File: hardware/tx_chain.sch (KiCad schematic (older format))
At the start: 28 parts

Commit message: honed multiple schematics
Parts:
- added D? (x2): BAT83, symbol D_Schottky
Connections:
- net +Vlogic: now also D?.1 (K)
- net GND: now also D?.2 (A); no longer T?.4 (SB)
- net joku_adc: now also C?.1
- net at C?.1, C?.1, T?.5 (SC): now also T?.4 (SB)
- net at Q?.3 (S), R?.1, R?.1: no longer C?.1
- new net: D?.1 (K), D?.2 (A)
- no-connect marks 0 -> 1
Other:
- moved on the sheet: C?, D?, L?, Q?, R?, T?, U?

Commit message: Added RX chain. also modified and cleand up other schemas
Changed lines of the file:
@@
 $Descr A4 11693 8268
 encoding utf-8
-Sheet 5 5
-Title ""
-Date ""
-Rev ""
-Comp ""
-Comment1 ""
+Sheet 5 7
+Title "TX chain"
+Date "2016-09-22"
+Rev "0.1"
+Comp "PRK - OH2TI"
+Comment1 "exla - OH2EHK"
 Comment2 ""
 Comment3 ""
@@
 	3250 3950 3250 4650
 Wire Wire Line
-	3050 4650 3250 4650
-Wire Wire Line
-	3250 4650 3950 4650
+	3050 4650 3950 4650
 Wire Wire Line
 	3050 4450 3400 4450
@@
 	3400 4450 3400 3750
 Wire Wire Line
-	3050 3750 3400 3750
-Wire Wire Line
-	3400 3750 3950 3750
-$Comp
-L GND #PWR?
+	3050 3750 3950 3750
+$Comp
+L GND #PWR018
 U 1 1 57E4343C
 P 3100 4100
-F 0 "#PWR?" H 3100 3850 50  0001 C CNN
+F 0 "#PWR018" H 3100 3850 50  0001 C CNN
 F 1 "GND" H 3100 3950 50  0000 C CNN
 F 2 "" H 3100 4100 50  0000 C CNN
@@
 	3100 3850 3100 4100
 $Comp
-L GND #PWR?
+L GND #PWR019
 U 1 1 57E4345E
 P 3100 4800
-F 0 "#PWR?" H 3100 4550 50  0001 C CNN
+F 0 "#PWR019" H 3100 4550 50  0001 C CNN
 F 1 "GND" H 3100 4650 50  0000 C CNN
 F 2 "" H 3100 4800 50  0000 C CNN
@@
 	1750 3750 2250 3750
 $Comp
-L +Vlogic #PWR?
+L +Vlogic #PWR020
 U 1 1 57E434AC
 P 2150 3550
-F 0 "#PWR?" H 2150 3350 50  0001 C CNN
+F 0 "#PWR020" H 2150 3350 50  0001 C CNN
 F 1 "+Vlogic" H 2150 3750 50  0000 C CNN
 F 2 "" H 2150 3550 50  0000 C CNN
@@
 $EndComp
 $Comp
-L +Vlogic #PWR?
+L +Vlogic #PWR021
 U 1 1 57E434C4
 P 2150 4250
-F 0 "#PWR?" H 2150 4050 50  0001 C CNN
+F 0 "#PWR021" H 2150 4050 50  0001 C CNN
 F 1 "+Vlogic" H 2150 4450 50  0000 C CNN
 F 2 "" H 2150 4250 50  0000 C CNN
@@
 $EndComp
 Wire Wire Line
-	3550 4100 3750 4100
-Wire Wire Line
-	3750 4100 3950 4100
-Wire Wire Line
-	3950 4100 3950 4150
-Wire Wire Line
-	3950 4150 3950 4350
+	3550 4100 3950 4100
+Wire Wire Line
+	3950 4100 3950 4350
 Connection ~ 3750 4100
 Connection ~ 3750 4400
 $Comp
-L GND #PWR?
+L GND #PWR022
 U 1 1 57E43B57
 P 3650 4450
-F 0 "#PWR?" H 3650 4200 50  0001 C CNN
+F 0 "#PWR022" H 3650 4200 50  0001 C CNN
 F 1 "GND" H 3650 4300 50  0000 C CNN
 F 2 "" H 3650 4450 50  0000 C CNN
@@
 Connection ~ 3650 4400
 $Comp
-L GND #PWR?
+L GND #PWR023
 U 1 1 57E43B98
 P 5100 4800
-F 0 "#PWR?" H 5100 4550 50  0001 C CNN
+F 0 "#PWR023" H 5100 4550 50  0001 C CNN
 F 1 "GND" H 5100 4650 50  0000 C CNN
 F 2 "" H 5100 4800 50  0000 C CNN
@@
 $EndComp
 Wire Wire Line
-	4750 4450 5100 4450
-Wire Wire Line
-	5100 4450 5700 4450
+	4750 4450 5700 4450
 Wire Wire Line
 	5700 4150 5700 4050
 Wire Wire Line
-	5600 4050 5700 4050
-Wire Wire Line
-	5700 4050 5800 4050
+	5600 4050 5800 4050
 $Comp
 L C C?
@@
 $EndComp
 Wire Wire Line
-	6100 4050 6200 4050
-Wire Wire Line
-	6200 4050 6300 4050
+	6100 4050 6300 4050
 $Comp
 L R R?
@@
 Connection ~ 5100 4450
 $Comp
-L GND #PWR?
+L GND #PWR024
 U 1 1 57E44284
 P 6600 4800
-F 0 "#PWR?" H 6600 4550 50  0001 C CNN
+F 0 "#PWR024" H 6600 4550 50  0001 C CNN
 F 1 "GND" H 6600 4650 50  0000 C CNN
 F 2 "" H 6600 4800 50  0000 C CNN
@@
 	6600 4350 6600 4250
 $Comp
-L Vin #Vin?
+L Vin #Vin025
 U 1 1 57E4514D
 P 6600 3050
-F 0 "#Vin?" H 6750 3100 60  0001 C CNN
+F 0 "#Vin025" H 6750 3100 60  0001 C CNN
 F 1 "Vin" H 6450 3100 60  0000 C CNN
 F 2 "" H 6600 3050 60  0001 C CNN
@@
 $EndComp
 $Comp
-L GND #PWR?
+L GND #PWR026
 U 1 1 57E451F7
 P 6850 3550
-F 0 "#PWR?" H 6850 3300 50  0001 C CNN
+F 0 "#PWR026" H 6850 3300 50  0001 C CNN
 F 1 "GND" H 6850 3400 50  0000 C CNN
 F 2 "" H 6850 3550 50  0000 C CNN
@@
 	6850 3500 6850 3550
 Wire Wire Line
-	6600 3500 6600 3800
-Wire Wire Line
-	6600 3800 6600 3850
+	6600 3500 6600 3850
 $Comp
 L C C?
@@
 $EndComp
 Wire Wire Line
-	7850 3800 7950 3800
-Wire Wire Line
-	7950 3800 8050 3800
+	7850 3800 8050 3800
 Wire Wire Line
 	7950 3800 7950 4050
 Wire Wire Line
-	7350 3800 7450 3800
-Wire Wire Line
-	7450 3800 7550 3800
+	7350 3800 7550 3800
 $Comp
 L R R?
@@
 Connection ~ 7950 3800
 Wire Wire Line
-	8100 3500 8350 3500
-Wire Wire Line
-	8350 3500 9100 3500
-Wire Wire Line
-	9100 3500 9200 3500
-Wire Wire Line
-	8350 3400 8350 3500
-Wire Wire Line
-	8350 3500 8350 3600
+	8100 3500 9200 3500
+Wire Wire Line
+	8350 3400 8350 3600
 $Comp
 L INDUCTOR L?
@@
 $EndComp
 $Comp
-L GND #PWR?
+L GND #PWR027
 U 1 1 57E458EE
 P 8100 3150
-F 0 "#PWR?" H 8100 2900 50  0001 C CNN
+F 0 "#PWR027" H 8100 2900 50  0001 C CNN
 F 1 "GND" H 8100 3000 50  0000 C CNN
 F 2 "" H 8100 3150 50  0000 C CNN
@@
 $EndComp
 $Comp
-L Vin #Vin?
+L Vin #Vin028
 U 1 1 57E45ADD
 P 8350 2200
-F 0 "#Vin?" H 8500 2250 60  0001 C CNN
+F 0 "#Vin028" H 8500 2250 60  0001 C CNN
 F 1 "Vin" H 8200 2250 60  0000 C CNN
 F 2 "" H 8350 2200 60  0001 C CNN
@@
 $EndComp
 $Comp
-L GND #PWR?
+L GND #PWR029
 U 1 1 57E45E2D
 P 8350 4900
-F 0 "#PWR?" H 8350 4650 50  0001 C CNN
+F 0 "#PWR029" H 8350 4650 50  0001 C CNN
 F 1 "GND" H 8350 4750 50  0000 C CNN
 F 2 "" H 8350 4900 50  0000 C CNN
@@
 Connection ~ 9900 3500
 $Comp
-L GND #PWR?
+L GND #PWR030
 U 1 1 57E465CB
 P 9500 4100
-F 0 "#PWR?" H 9500 3850 50  0001 C CNN
+F 0 "#PWR030" H 9500 3850 50  0001 C CNN
 F 1 "GND" H 9500 3950 50  0000 C CNN
 F 2 "" H 9500 4100 50  0000 C CNN
@@
 $EndComp
 Wire Wire Line
-	9100 3900 9500 3900
-Wire Wire Line
-	9500 3900 9900 3900
+	9100 3900 9900 3900
 Wire Wire Line
 	9500 4100 9500 3900
@@
 	7950 5250 8300 5250
 Wire Wire Line
-	9800 3500 9900 3500
-Wire Wire Line
-	9900 3500 10200 3500
+	9800 3500 10200 3500
 Text HLabel 10200 3500 2    60   Output ~ 0
 TX_CHAIN
@@
 $EndComp
 $Comp
-L GND #PWR?
+L GND #PWR031
 U 1 1 57E471D5
 P 5700 3800
-F 0 "#PWR?" H 5700 3550 50  0001 C CNN
+F 0 "#PWR031" H 5700 3550 50  0001 C CNN
 F 1 "GND" H 5700 3650 50  0000 C CNN
 F 2 "" H 5700 3800 50  0000 C CNN
@@
 $EndComp
 Wire Wire Line
-	8750 4600 8850 4600
-Wire Wire Line
-	8850 4600 9450 4600
+	8750 4600 9450 4600
 Connection ~ 8850 4600
 Wire Wire Line
@@
 NoConn ~ 5750 3150
 Wire Wire Line
-	3550 4400 3650 4400
-Wire Wire Line
-	3650 4400 3750 4400
+	3550 4400 3750 4400
 Connection ~ 3950 4150
 Wire Wire Line
 	8350 4600 8450 4600
 $Comp
-L +Vlogic #PWR?
+L +Vlogic #PWR032
 U 1 1 57E47CF4
 P 9150 4300
-F 0 "#PWR?" H 9150 4100 50  0001 C CNN
+F 0 "#PWR032" H 9150 4100 50  0001 C CNN
 F 1 "+Vlogic" H 9150 4500 50  0000 C CNN
 F 2 "" H 9150 4300 50  0000 C CNN
@@
 $EndComp
 $Comp
-L GND #PWR?
+L GND #PWR033
 U 1 1 57E47E8B
 P 9150 4900
-F 0 "#PWR?" H 9150 4650 50  0001 C CNN
+F 0 "#PWR033" H 9150 4650 50  0001 C CNN
 F 1 "GND" H 9150 4750 50  0000 C CNN
 F 2 "" H 9150 4900 50  0000 C CNN

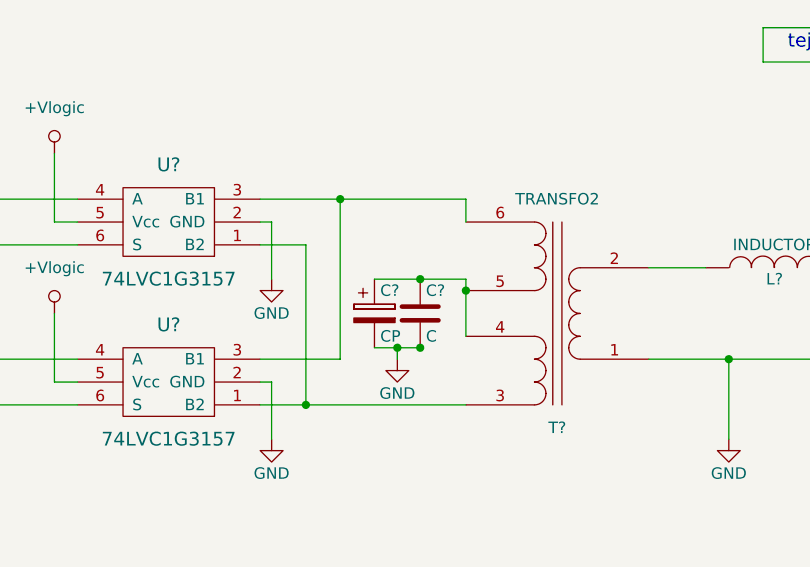
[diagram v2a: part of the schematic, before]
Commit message: Added biases for RX and TX chains where needed
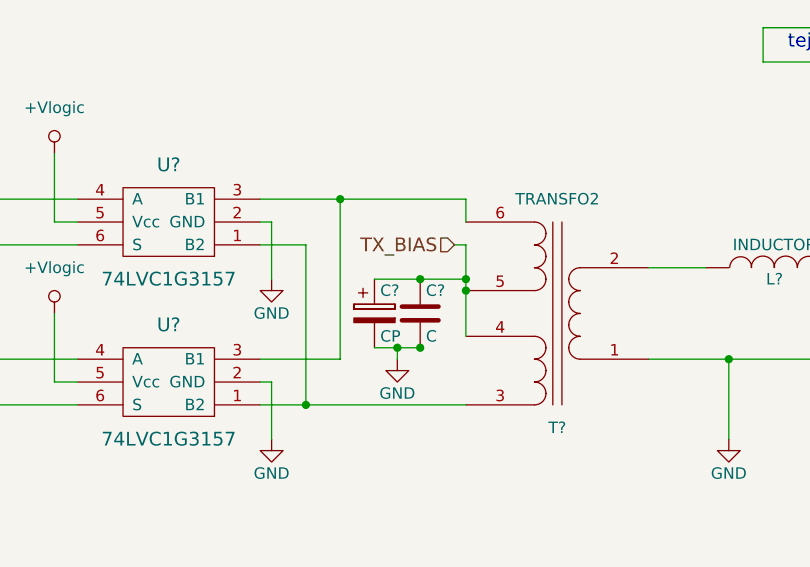
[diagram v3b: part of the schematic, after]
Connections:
- net TX_BIAS: now reaches C?.1, C?.1, T?.4 (SB), T?.5 (SC)
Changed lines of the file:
@@
 Comp "PRK - OH2TI"
 Comment1 "exla - OH2EHK"
-Comment2 ""
+Comment2 "tejeez - OH2EAT"
 Comment3 ""
 Comment4 ""
@@
 	3550 4100 3950 4100
 Wire Wire Line
-	3950 4100 3950 4350
+	3950 3950 3950 4350
 Connection ~ 3750 4100
 Connection ~ 3750 4400
@@
 	1    0    0    -1
 $EndComp
+Text HLabel 3900 3950 0    60   Input ~ 0
+TX_BIAS
+Wire Wire Line
+	3900 3950 3950 3950
+Connection ~ 3950 4100
 $EndSCHEMATC

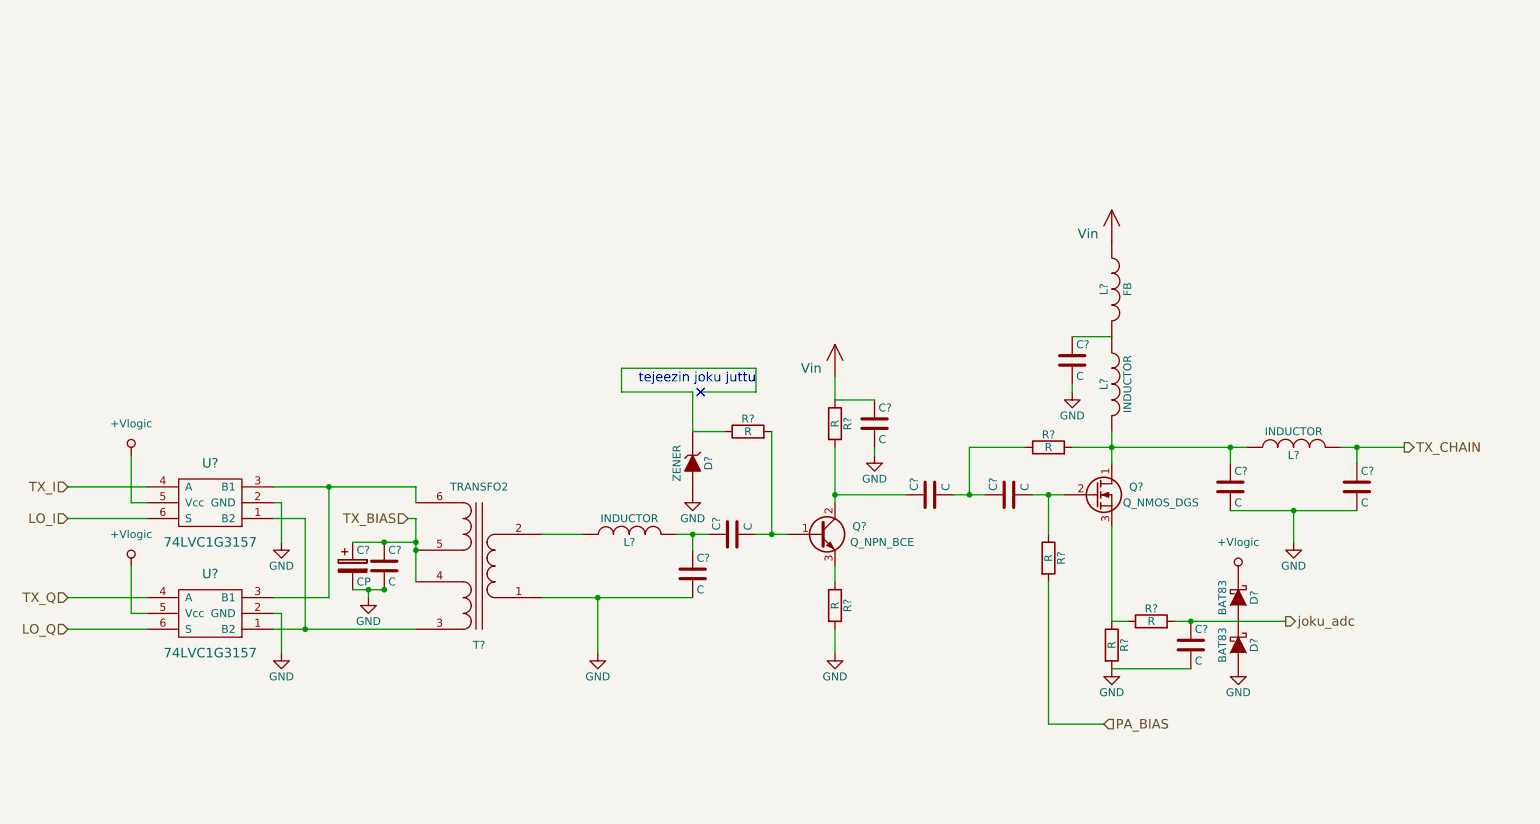
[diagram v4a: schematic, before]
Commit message: Allocated CPU some pins and made minor adjustments here and there
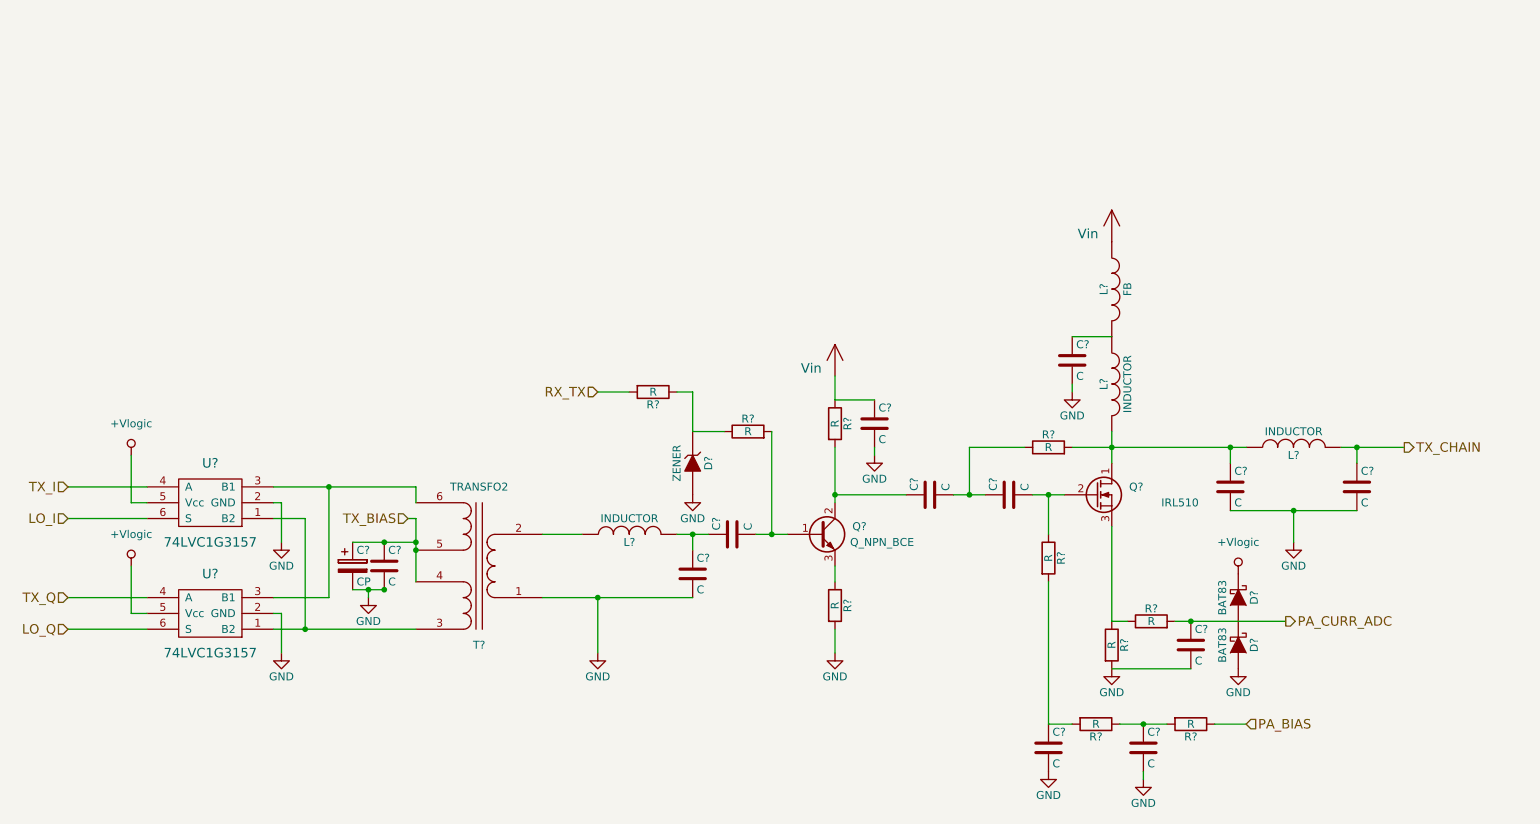
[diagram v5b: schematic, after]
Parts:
- added C? (x2): C, symbol C
- added R? (x3): R, symbol R
- Q?: value Q_NMOS_DGS -> IRL510
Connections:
- net GND: now also C?.2, C?.2
- net PA_BIAS: now also R?.1; no longer R?.2
- net at D?.1 (K), R?.1: now also R?.1
- net joku_adc renamed PA_CURR_ADC
- new net: C?.1, R?.2, R?.2
- new net: C?.1, R?.1, R?.2
- new net RX_TX: R?.2
- no-connect marks 1 -> 0
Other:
- note removed: "tejeezin joku juttu"
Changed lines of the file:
@@
 P 8250 3800
 F 0 "Q?" H 8550 3850 50  0000 R CNN
-F 1 "Q_NMOS_DGS" H 8900 3750 50  0000 R CNN
+F 1 "IRL510" H 8900 3750 50  0000 R CNN
 F 2 "" H 8450 3900 50  0000 C CNN
 F 3 "" H 8250 3800 50  0000 C CNN
@@
 	9500 4100 9500 3900
 Connection ~ 9500 3900
-Text HLabel 8300 5250 2    60   Input ~ 0
+Text HLabel 9200 5250 2    60   Input ~ 0
 PA_BIAS
 Wire Wire Line
 	7950 4350 7950 5250
 Wire Wire Line
-	7950 5250 8300 5250
+	7950 5250 8100 5250
 Wire Wire Line
 	9800 3500 10200 3500
@@
 	8850 4900 8350 4900
 Text HLabel 9450 4600 2    60   Output ~ 0
-joku_adc
+PA_CURR_ADC
 Wire Wire Line
 	5700 3400 5700 3150
-Text Notes 6100 3100 2    60   ~ 0
-tejeezin joku juttu
-Wire Wire Line
-	5700 3150 5250 3150
-Wire Wire Line
-	5250 3150 5250 3000
-Wire Wire Line
-	5250 3000 6100 3000
-Wire Wire Line
-	6100 3000 6100 3150
-Wire Wire Line
-	6100 3150 5750 3150
-NoConn ~ 5750 3150
 Wire Wire Line
 	3550 4400 3750 4400
@@
 	3900 3950 3950 3950
 Connection ~ 3950 4100
+$Comp
+L C C?
+U 1 1 57EBA4F1
+P 7950 5400
+F 0 "C?" H 7975 5500 50  0000 L CNN
+F 1 "C" H 7975 5300 50  0000 L CNN
+F 2 "" H 7988 5250 50  0000 C CNN
+F 3 "" H 7950 5400 50  0000 C CNN
+	1    7950 5400
+	1    0    0    -1
+$EndComp
+$Comp
+L GND #PWR?
+U 1 1 57EBA5D8
+P 7950 5550
+F 0 "#PWR?" H 7950 5300 50  0001 C CNN
+F 1 "GND" H 7950 5400 50  0000 C CNN
+F 2 "" H 7950 5550 50  0000 C CNN
+F 3 "" H 7950 5550 50  0000 C CNN
+	1    7950 5550
+	1    0    0    -1
+$EndComp
+$Comp
+L C C?
+U 1 1 57EBA62A
+P 8550 5400
+F 0 "C?" H 8575 5500 50  0000 L CNN
+F 1 "C" H 8575 5300 50  0000 L CNN
+F 2 "" H 8588 5250 50  0000 C CNN
+F 3 "" H 8550 5400 50  0000 C CNN
+	1    8550 5400
+	1    0    0    -1
+$EndComp
+$Comp
+L GND #PWR?
+U 1 1 57EBA6B5
+P 8550 5600
+F 0 "#PWR?" H 8550 5350 50  0001 C CNN
+F 1 "GND" H 8550 5450 50  0000 C CNN
+F 2 "" H 8550 5600 50  0000 C CNN
+F 3 "" H 8550 5600 50  0000 C CNN
+	1    8550 5600
+	1    0    0    -1
+$EndComp
+Wire Wire Line
+	8550 5600 8550 5550
+$Comp
+L R R?
+U 1 1 57EBAB97
+P 8250 5250
+F 0 "R?" V 8330 5250 50  0000 C CNN
+F 1 "R" V 8250 5250 50  0000 C CNN
+F 2 "" V 8180 5250 50  0000 C CNN
+F 3 "" H 8250 5250 50  0000 C CNN
+	1    8250 5250
+	0    1    1    0
+$EndComp
+Wire Wire Line
+	8400 5250 8700 5250
+$Comp
+L R R?
+U 1 1 57EBAD40
+P 8850 5250
+F 0 "R?" V 8930 5250 50  0000 C CNN
+F 1 "R" V 8850 5250 50  0000 C CNN
+F 2 "" V 8780 5250 50  0000 C CNN
+F 3 "" H 8850 5250 50  0000 C CNN
+	1    8850 5250
+	0    1    1    0
+$EndComp
+Connection ~ 8550 5250
+Wire Wire Line
+	9000 5250 9200 5250
+$Comp
+L R R?
+U 1 1 57EBC6D8
+P 5450 3150
+F 0 "R?" V 5530 3150 50  0000 C CNN
+F 1 "R" V 5450 3150 50  0000 C CNN
+F 2 "" V 5380 3150 50  0000 C CNN
+F 3 "" H 5450 3150 50  0000 C CNN
+	1    5450 3150
+	0    1    1    0
+$EndComp
+Wire Wire Line
+	5700 3150 5600 3150
+Text HLabel 5100 3150 0    60   Input ~ 0
+RX_TX
+Wire Wire Line
+	5100 3150 5300 3150
 $EndSCHEMATC

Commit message: Made some minor adjustments and replotted schematic .pdf
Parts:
- removed D? (x2): BAT83, symbol D_Schottky
- removed L?: FB, symbol INDUCTOR
- added D?: BAT54SLT, symbol D_Schottky_x2_Serial_AKC
- added FB?: FILTER, symbol FILTER
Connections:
- net +Vlogic: now also D?.2 (K)
- net GND: now also D?.1 (A)
- net PA_CURR_ADC: now also D?.3 (common); no longer R?.2
- net at C?.1, L?.1: now also FB?.2
